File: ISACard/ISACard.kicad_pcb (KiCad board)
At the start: 2 copper layers, 171.5 x 95.9 mm, 95 parts, among them J1 Bus_ISA_8bit, J2 ICSP, J3 WIZNET, J4 SERCON, J5 Conn_01x16, Q1 2N3904, SW1 SW_Push, U1 74LS86, U10 28C256, U11 ATmega328P-P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

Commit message: Added labels
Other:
- board text added: "IO2"
- board text added: "IO3"
- board text added: "IO4"
- board text added: "IO5"
- board text added: "IO6"
- board text added: "IO7"
- board text added: "IO8"
- board text added: "IO9"
- board text added: "M12"
- board text added: "M13"
- board text added: "M14"
- board text added: "M15"
- board text added: "M16"
- board text added: "M17"
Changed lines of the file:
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@@
+    (effects (font (size 1 1) (thickness 0.15)))
+  )
+  (gr_text "IO3" (at 126.55 122.24) (layer "F.SilkS")
     (effects (font (size 1 1) (thickness 0.15)))
   )
@@
     (effects (font (size 1 1) (thickness 0.15)))
   )
+  (gr_text "M15" (at 159.68 89.61) (layer "F.SilkS")
+    (effects (font (size 1 1) (thickness 0.15)))
+  )
   (gr_text "ATMEGA328P" (at 77.42 91.69) (layer "F.SilkS")
     (effects (font (size 1 1) (thickness 0.15)))
@@
     (effects (font (size 1 1) (thickness 0.15)))
   )
+  (gr_text "M13" (at 151.86 89.65) (layer "F.SilkS")
+    (effects (font (size 1 1) (thickness 0.15)))
+  )
   (gr_text "PB2" (at 107.69 139.89 90) (layer "F.SilkS")
     (effects (font (size 1 1) (thickness 0.15)))
@@
     (effects (font (size 1 1) (thickness 0.15)))
   )
+  (gr_text "IO2" (at 122.86 122.3) (layer "F.SilkS")
+    (effects (font (size 1 1) (thickness 0.15)))
+  )
   (gr_text "1" (at 165.39 85.51) (layer "F.SilkS")
     (effects (font (size 1 1) (thickness 0.15)))
   )
   (gr_text "74HCT32" (at 150.27 106.66) (layer "F.SilkS")
+    (effects (font (size 1 1) (thickness 0.15)))
+  )
+  (gr_text "M12" (at 148.16 89.61) (layer "F.SilkS")
+    (effects (font (size 1 1) (thickness 0.15)))
+  )
+  (gr_text "IO4" (at 130.55 122.3) (layer "F.SilkS")
     (effects (font (size 1 1) (thickness 0.15)))
   )
@@
     (effects (font (size 1 1) (thickness 0.15)))
   )
+  (gr_text "M14" (at 155.98 89.65) (layer "F.SilkS")
+    (effects (font (size 1 1) (thickness 0.15)))
+  )
+  (gr_text "IO8" (at 196.23 121.73) (layer "F.SilkS")
+    (effects (font (size 1 1) (thickness 0.15)))
+  )
+  (gr_text "IO9" (at 200.3 121.72) (layer "F.SilkS")
+    (effects (font (size 1 1) (thickness 0.15)))
+  )
+  (gr_text "IO5" (at 134.65 122.21) (layer "F.SilkS")
+    (effects (font (size 1 1) (thickness 0.15)))
+  )
   (gr_text "MISO" (at 95.32 67.85) (layer "F.SilkS")
     (effects (font (size 1 1) (thickness 0.15)))
@@
   )
   (gr_text "SDA" (at 74.79 70.13) (layer "F.SilkS")
+    (effects (font (size 1 1) (thickness 0.15)))
+  )
+  (gr_text "M16" (at 213.62 88.82) (layer "F.SilkS")
     (effects (font (size 1 1) (thickness 0.15)))
   )
@@
     (effects (font (size 1 1) (thickness 0.15)))
   )
+  (gr_text "IO7" (at 192.41 121.68) (layer "F.SilkS")
+    (effects (font (size 1 1) (thickness 0.15)))
+  )
   (gr_text "1" (at 165.46 98.92) (layer "F.SilkS")
     (effects (font (size 1 1) (thickness 0.15)))
   )
+  (gr_text "IO6" (at 188.44 121.68) (layer "F.SilkS")
+    (effects (font (size 1 1) (thickness 0.15)))
+  )
+  (gr_text "M17" (at 217.32 88.78) (layer "F.SilkS")
+    (effects (font (size 1 1) (thickness 0.15)))
+  )

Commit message: Added gerber files and CS/CS2 to feature connector
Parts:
- added R34: 470R, Resistor_THT:R_Axial_DIN0207_L6.3mm_D2.5mm_P7.62mm_Horizontal, F.Cu at (74.6, 82.2)
- added R35: 470R, Resistor_THT:R_Axial_DIN0207_L6.3mm_D2.5mm_P7.62mm_Horizontal, F.Cu at (77.8, 82.2)
- J3: value WIZNET -> EXTSPI
- moved C2 3.95 mm to (71.6, 88.2)
- moved R20 1.84 mm to (68.4, 83.2)
- moved Q1 1.72 mm to (56.1, 86.4)
- moved R19 1.57 mm to (65.3, 90.8)
- moved D2 0.92 mm to (64.3, 77.7)
- moved R18 0.87 mm to (64.3, 80.6)
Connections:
- J3 pad 7: unconnected-(J3-Pad7) -> Net-(J3-Pad7)
- J3 pad 9: unconnected-(J3-Pad9) -> Net-(J3-Pad9)
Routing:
- net CS2: track 19.0 -> 46.1 mm
- net Net-(J3-Pad7): track 0.00 -> 21.3 mm
- net CS: track 58.6 -> 79.2 mm
- net Net-(J3-Pad9): track 0.00 -> 16.6 mm
- net Net-(C2-Pad1): track 6.05 -> 10.9 mm
- net Net-(C1-Pad1): track 78.1 -> 81.0 mm
- net Net-(J4-Pad5): track 27.9 -> 29.7 mm
- net ARESET: track 79.9 -> 78.0 mm
- net Net-(J4-Pad7): track 28.3 -> 30.1 mm
- net Net-(C5-Pad1): track 19.4 -> 17.8 mm
- net PC5: track 103.4 -> 102.1 mm
- net APC5: track 37.7 -> 38.9 mm
- net PA0: track 61.9 -> 62.6 mm
- net PC4: track 109.9 -> 109.2 mm
- net PC6: track 94.6 -> 94.0 mm
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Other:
- board text added: "CS2"
- board text added: "CS3"

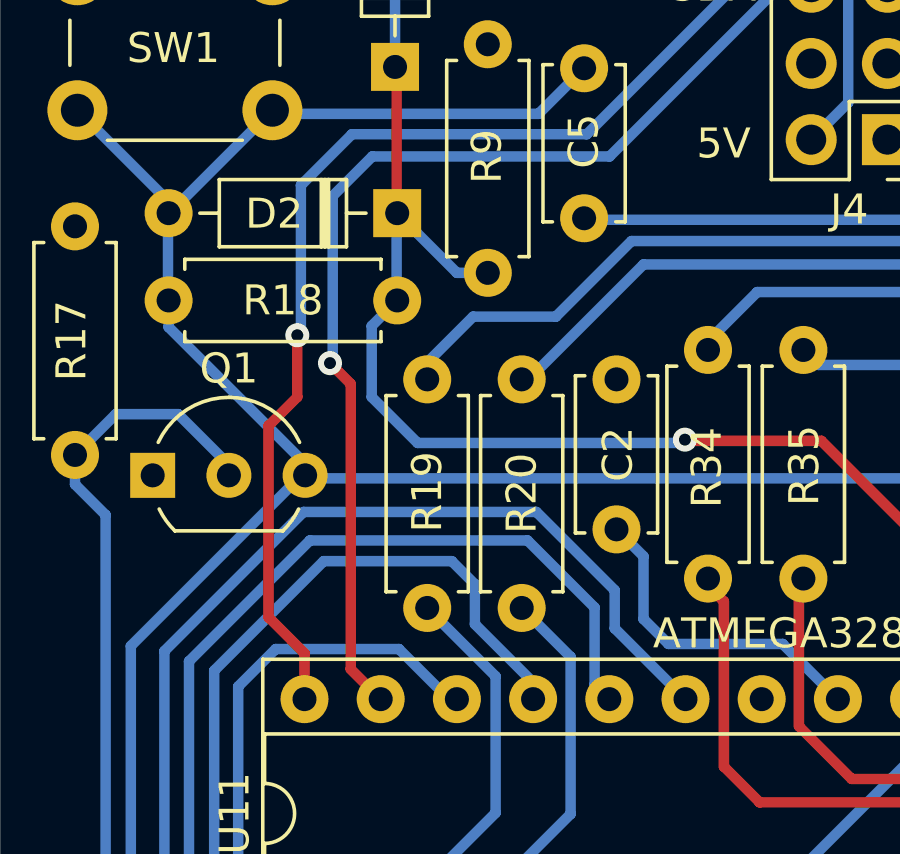
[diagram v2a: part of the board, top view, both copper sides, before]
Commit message: Added external SD card board
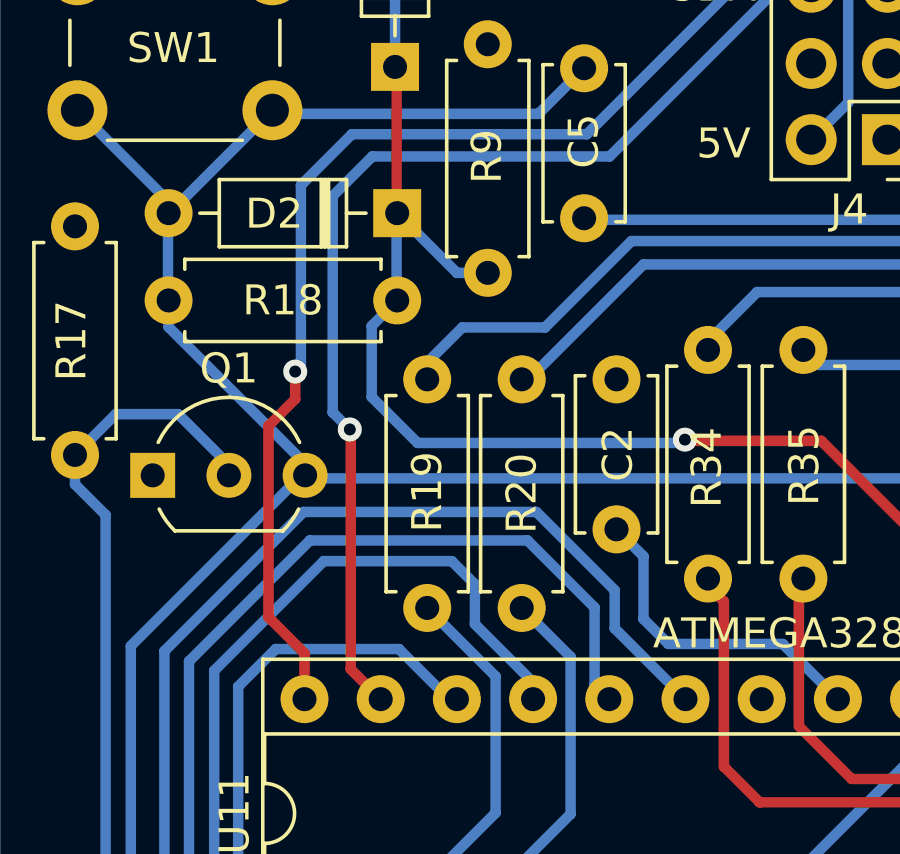
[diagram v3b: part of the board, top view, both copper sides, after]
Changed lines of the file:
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@@
   (segment (start 94.02 72.94) (end 91.76 72.94) (width 0.35) (layer "B.Cu") (net 124))
   (segment (start 175.186 64.932) (end 175.186 67.726) (width 0.35) (layer "B.Cu") (net 125))
+  (segment (start 83.19 77.23) (end 83.19 71.29) (width 0.35) (layer "B.Cu") (net 128))
+  (segment (start 65.26 83.22) (end 65.26 82.66) (width 0.35) (layer "B.Cu") (net 128))
+  (segment (start 83.19 71.29) (end 82.05 70.15) (width 0.35) (layer "B.Cu") (net 128))
+  (segment (start 72.07 78.61) (end 81.81 78.61) (width 0.35) (layer "B.Cu") (net 128))
+  (segment (start 65.26 82.66) (end 66.43 81.49) (width 0.35) (layer "B.Cu") (net 128))
+  (segment (start 82.05 70.15) (end 80.6 70.15) (width 0.35) (layer "B.Cu") (net 128))
   (segment (start 81.81 78.61) (end 83.19 77.23) (width 0.35) (layer "B.Cu") (net 128))
-  (segment (start 72.07 78.61) (end 81.81 78.61) (width 0.35) (layer "B.Cu") (net 128))
-  (segment (start 69.55 81.13) (end 72.07 78.61) (width 0.35) (layer "B.Cu") (net 128))
-  (segment (start 83.19 77.23) (end 83.19 71.29) (width 0.35) (layer "B.Cu") (net 128))
-  (segment (start 83.19 71.29) (end 82.05 70.15) (width 0.35) (layer "B.Cu") (net 128))
-  (segment (start 82.05 70.15) (end 80.6 70.15) (width 0.35) (layer "B.Cu") (net 128))
-  (segment (start 66.79 81.13) (end 69.55 81.13) (width 0.35) (layer "B.Cu") (net 128))
-  (segment (start 65.26 83.22) (end 65.26 82.66) (width 0.35) (layer "B.Cu") (net 128))
-  (segment (start 65.26 82.66) (end 66.79 81.13) (width 0.35) (layer "B.Cu") (net 128))
-  (segment (start 62.02 82.68) (end 62.71 83.37) (width 0.35) (layer "F.Cu") (net 129))
+  (segment (start 66.43 81.49) (end 69.19 81.49) (width 0.35) (layer "B.Cu") (net 128))
+  (segment (start 69.19 81.49) (end 72.07 78.61) (width 0.35) (layer "B.Cu") (net 128))
+  (segment (start 62.68 84.89) (end 62.71 84.92) (width 0.35) (layer "F.Cu") (net 129))
+  (segment (start 62.71 84.92) (end 62.71 92.88) (width 0.35) (layer "F.Cu") (net 129))
   (segment (start 62.71 92.88) (end 63.71 93.88) (width 0.35) (layer "F.Cu") (net 129))
-  (segment (start 62.71 83.37) (end 62.71 92.88) (width 0.35) (layer "F.Cu") (net 129))
-  (via (at 62.02 82.68) (size 0.8) (drill 0.4) (layers "F.Cu" "B.Cu") (net 129))
+  (via (at 62.68 84.89) (size 0.8) (drill 0.4) (layers "F.Cu" "B.Cu") (net 129))
+  (segment (start 62.11 77.11) (end 63.43 75.79) (width 0.35) (layer "B.Cu") (net 129))
+  (segment (start 62.11 84.32) (end 62.11 77.11) (width 0.35) (layer "B.Cu") (net 129))
+  (segment (start 76.87 70.26) (end 77.95 70.26) (width 0.35) (layer "B.Cu") (net 129))
   (segment (start 71.34 75.79) (end 76.87 70.26) (width 0.35) (layer "B.Cu") (net 129))
   (segment (start 63.43 75.79) (end 71.34 75.79) (width 0.35) (layer "B.Cu") (net 129))
-  (segment (start 62.11 82.59) (end 62.11 77.11) (width 0.35) (layer "B.Cu") (net 129))
-  (segment (start 62.11 77.11) (end 63.43 75.79) (width 0.35) (layer "B.Cu") (net 129))
-  (segment (start 62.02 82.68) (end 62.11 82.59) (width 0.35) (layer "B.Cu") (net 129))
+  (segment (start 62.68 84.89) (end 62.11 84.32) (width 0.35) (layer "B.Cu") (net 129))
   (segment (start 77.95 70.26) (end 78.06 70.15) (width 0.35) (layer "B.Cu") (net 129))
-  (segment (start 76.87 70.26) (end 77.95 70.26) (width 0.35) (layer "B.Cu") (net 129))
   (segment (start 82.18 79.39) (end 83.94 77.63) (width 0.35) (layer "B.Cu") (net 130))
   (segment (start 83.94 77.63) (end 83.94 69.42) (width 0.35) (layer "B.Cu") (net 130))
@@
   (segment (start 68.41 83.22) (end 68.64 83.22) (width 0.35) (layer "B.Cu") (net 130))
   (segment (start 68.64 83.22) (end 72.47 79.39) (width 0.35) (layer "B.Cu") (net 130))
-  (segment (start 60.93 81.75) (end 60.93 83.81) (width 0.35) (layer "F.Cu") (net 131))
   (segment (start 59.97 91.15) (end 61.17 92.35) (width 0.35) (layer "F.Cu") (net 131))
-  (segment (start 60.93 83.81) (end 59.97 84.77) (width 0.35) (layer "F.Cu") (net 131))
+  (segment (start 60.86 83.88) (end 59.97 84.77) (width 0.35) (layer "F.Cu") (net 131))
   (segment (start 59.97 84.77) (end 59.97 91.15) (width 0.35) (layer "F.Cu") (net 131))
   (segment (start 61.17 92.35) (end 61.17 93.88) (width 0.35) (layer "F.Cu") (net 131))
-  (via (at 60.93 81.75) (size 0.8) (drill 0.4) (layers "F.Cu" "B.Cu") (net 131))
-  (segment (start 60.93 81.75) (end 61.05 81.63) (width 0.35) (layer "B.Cu") (net 131))
+  (segment (start 60.86 82.96) (end 60.86 83.88) (width 0.35) (layer "F.Cu") (net 131))
+  (via (at 60.86 82.96) (size 0.8) (drill 0.4) (layers "F.Cu" "B.Cu") (net 131))
+  (segment (start 70.58 75.05) (end 78.02 67.61) (width 0.35) (layer "B.Cu") (net 131))
+  (segment (start 61.05 82.77) (end 61.05 76.75) (width 0.35) (layer "B.Cu") (net 131))
+  (segment (start 62.75 75.05) (end 70.58 75.05) (width 0.35) (layer "B.Cu") (net 131))
   (segment (start 61.05 76.75) (end 62.75 75.05) (width 0.35) (layer "B.Cu") (net 131))
-  (segment (start 62.75 75.05) (end 70.58 75.05) (width 0.35) (layer "B.Cu") (net 131))
-  (segment (start 61.05 81.63) (end 61.05 76.75) (width 0.35) (layer "B.Cu") (net 131))
   (segment (start 78.02 67.61) (end 78.06 67.61) (width 0.35) (layer "B.Cu") (net 131))
-  (segment (start 70.58 75.05) (end 78.02 67.61) (width 0.35) (layer "B.Cu") (net 131))
+  (segment (start 60.86 82.96) (end 61.05 82.77) (width 0.35) (layer "B.Cu") (net 131))
   (segment (start 54.54 106.67) (end 54.54 87.74) (width 0.35) (layer "B.Cu") (net 132))
   (segment (start 53.52 86.72) (end 54.54 87.74) (width 0.35) (layer "B.Cu") (net 132))

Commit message: Moved around some traces
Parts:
- R10: footprint Resistor_THT:R_Axial_DIN0207_L6.3mm_D2.5mm_P7.62mm_Horizontal -> Resistor_THT:R_Axial_DIN0207_L6.3mm_D2.5mm_P10.16mm_Horizontal
- R34, R35: value 470R -> 4k7
- moved JP18 0.77 mm to (142.6, 93.3)
- moved C13 0.33 mm to (147.0, 103.5)
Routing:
- net PA0: track 62.6 -> 64.1 mm
- net PC4: track 109.2 -> 110.5 mm
- net PC5: track 102.1 -> 103.3 mm
- net PC6: track 94.0 -> 95.1 mm
- net PA1: track 59.7 -> 60.7 mm
- net Net-(Q1-Pad2): track 36.8 -> 35.8 mm
- net PC7: track 82.7 -> 83.7 mm
- net ARESET: track 78.0 -> 79.0 mm
- net +5V: track 634.9 -> 634.1 mm
- net IOR: track 138.2 -> 137.5 mm
- net PA2: track 43.9 -> 44.6 mm
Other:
- board text added: "32K"
- board text added: "8K"
- board text added: "FLASH"
- board text added: "ICSP"
- board text added: "ICSP PWR"
- board text added: "RDONLY"
- board text added: "VDROP"

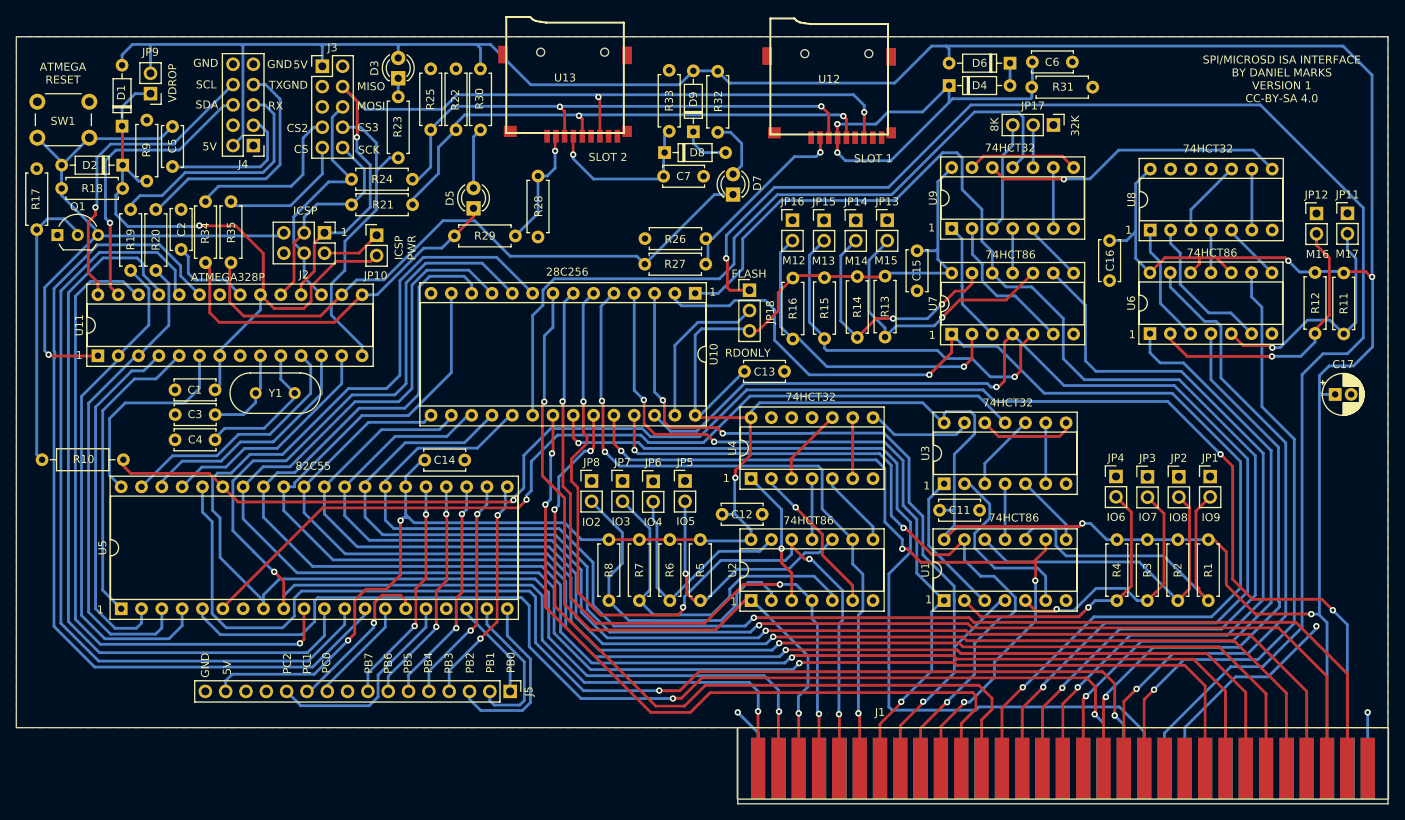
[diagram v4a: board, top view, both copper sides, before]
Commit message: Added 16k/32k jumper
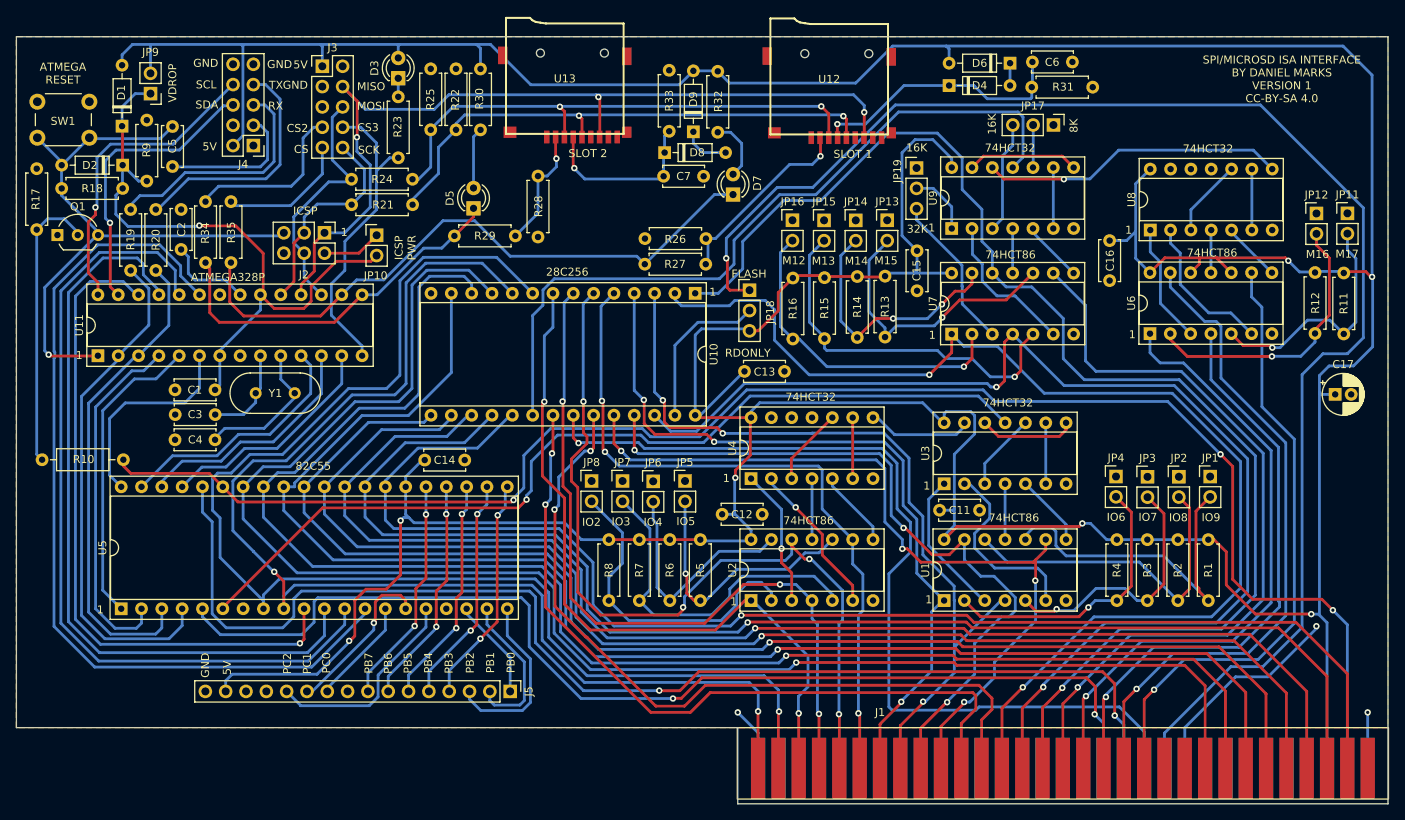
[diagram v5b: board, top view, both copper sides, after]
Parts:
- added JP19: Jumper_3_Open, Connector_PinHeader_2.54mm:PinHeader_1x03_P2.54mm_Vertical, F.Cu at (163.5, 78.0)
- moved U13 0.11 mm to (119.5, 75.0)
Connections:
- U9 pad 1: Net-(U7-Pad3) -> Net-(U9-Pad1)
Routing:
- net Net-(C6-Pad2): track 54.2 -> 33.3 mm, vias 2 -> 1
- net Net-(U9-Pad1): track 0.00 -> 8.06 mm
- net +5V: track 634.1 -> 642.0 mm
- net Net-(U7-Pad3): track 15.3 -> 19.6 mm
- net A14: track 161.9 -> 163.7 mm
- net Net-(C7-Pad2): track 21.2 -> 21.8 mm
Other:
- board text added: "16K"
